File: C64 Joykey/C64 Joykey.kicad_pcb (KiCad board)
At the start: 2 copper layers, 99.7 x 74.9 mm, 47 parts, among them J1 Port_1, J2 Port_2, M1 Mounting, M2 Mounting, M3 Mounting, M4 Mounting, Q1 2N3904, SW1 FIRE1, SW2 FIRE2, SW3 FIRE3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

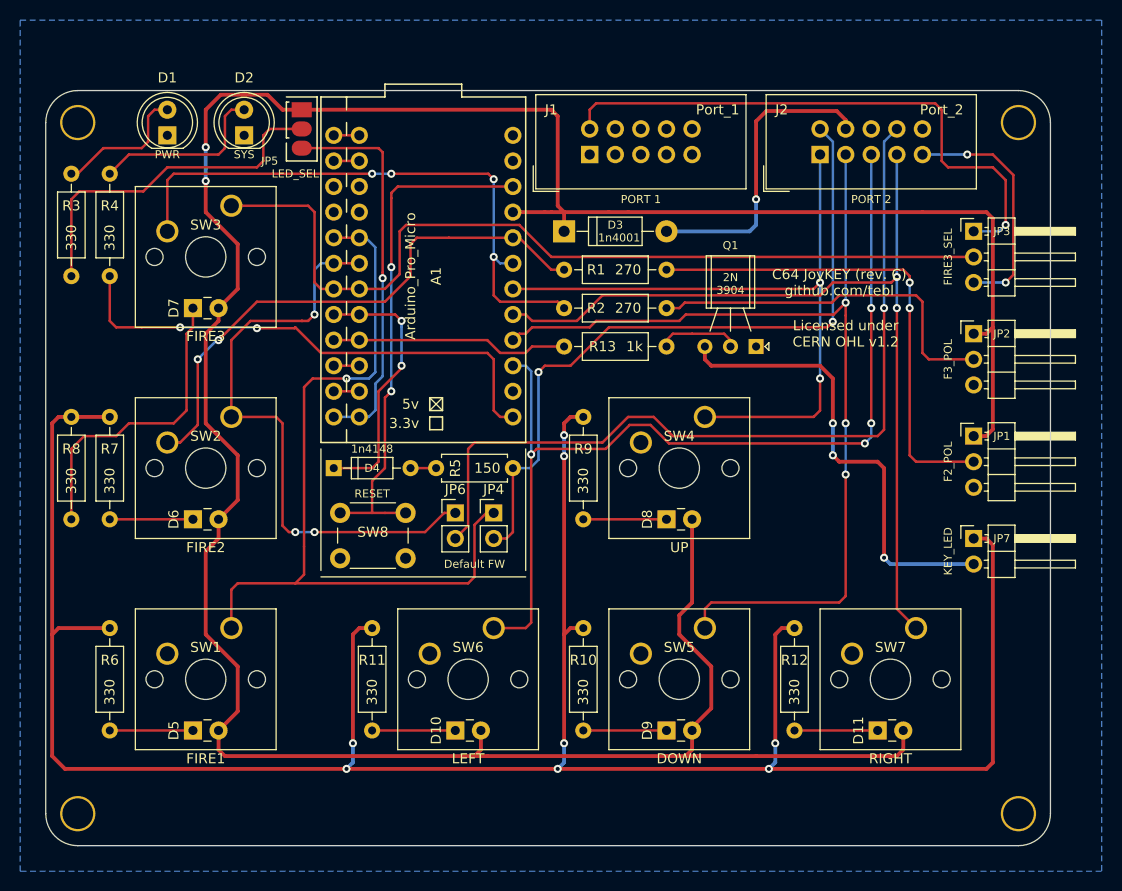
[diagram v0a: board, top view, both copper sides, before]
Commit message: Flipped MX-switches
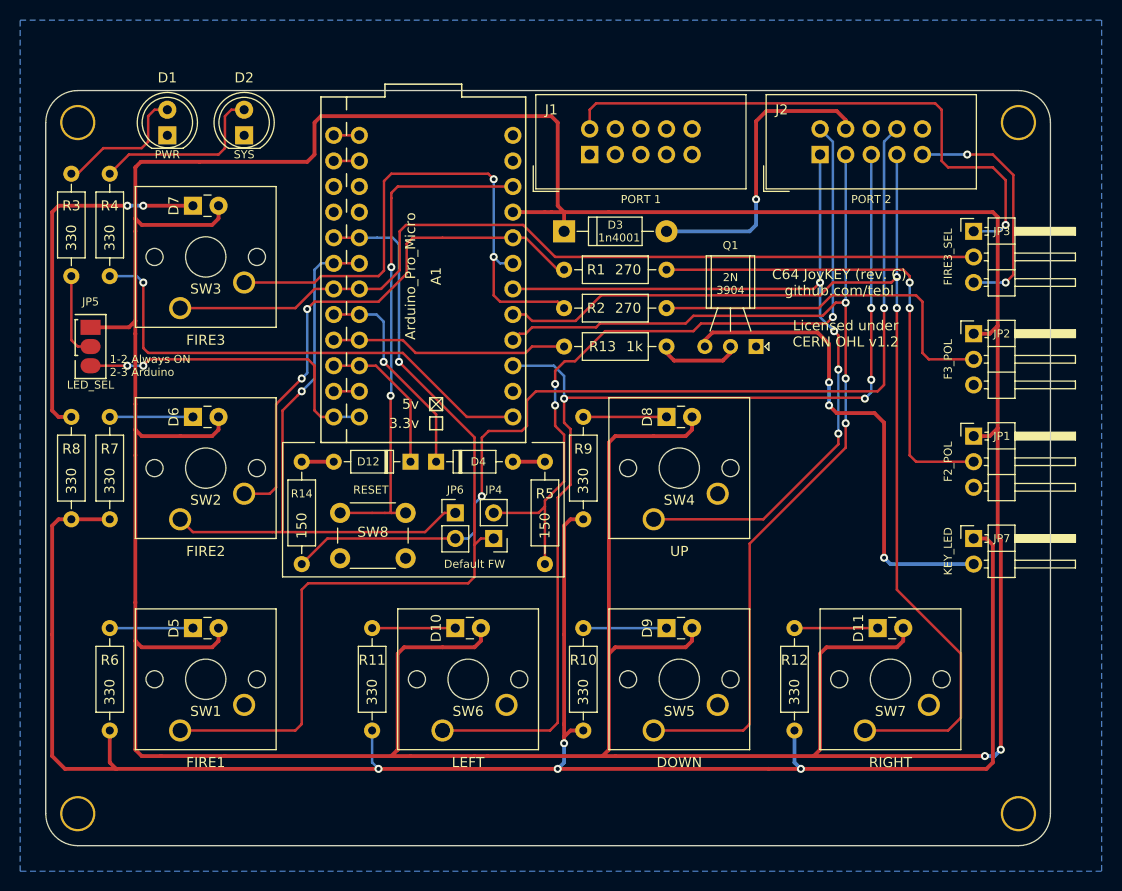
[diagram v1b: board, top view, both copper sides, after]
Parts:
- added D12: 1n4148, Diode_THT:D_DO-35_SOD27_P7.62mm_Horizontal, F.Cu at (177.2, 119.4)
- added R14: 150, Resistor_THT:R_Axial_DIN0207_L6.3mm_D2.5mm_P10.16mm_Horizontal, F.Cu at (166.4, 119.4)
- D4: footprint Diodes_THT:D_DO-35_SOD27_P7.62mm_Horizontal -> Diode_THT:D_DO-35_SOD27_P7.62mm_Horizontal
- R5: footprint Resistor_THT:R_Axial_DIN0207_L6.3mm_D2.5mm_P7.62mm_Horizontal -> Resistor_THT:R_Axial_DIN0207_L6.3mm_D2.5mm_P10.16mm_Horizontal
- moved JP5 30.1 mm to (145.4, 106.0)
- moved SW5 11.4 mm to (201.3, 146.1), turned to 180 degrees
- moved SW7 11.4 mm to (222.2, 146.1), turned to 180 degrees
- moved SW1 11.4 mm to (154.3, 146.1), turned to 180 degrees
- moved SW6 11.4 mm to (180.3, 146.1), turned to 180 degrees
- moved SW4 11.4 mm to (201.3, 125.1), turned to 180 degrees
- moved SW2 11.4 mm to (154.3, 125.1), turned to 180 degrees
- moved SW3 11.4 mm to (154.3, 104.1), turned to 180 degrees
- moved R5 10.8 mm to (190.5, 119.4), turned to 270 degrees
- moved D4 10.2 mm to (179.7, 119.4)
- moved D10 10.2 mm to (181.6, 135.9)
- moved D11 10.2 mm to (223.5, 135.9)
- moved D5 10.2 mm to (155.6, 135.9)
- moved D9 10.2 mm to (202.6, 135.9)
- moved R10 10.2 mm to (194.3, 135.9), turned to 270 degrees
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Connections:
- net Net-(A1-Pad12) renamed /PWR
- net Net-(A1-Pad13) renamed /SYS
- net Net-(A1-Pad9) renamed /UNDERGLOW
- A1 pad 10: Net-(A1-Pad10) -> /FIRE2_OUT
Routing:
- net VCC: track 292.3 -> 436.0 mm
- net Net-(JP7-Pad1): track 233.3 -> 187.7 mm, vias 8 -> 4
- net Net-(JP5-Pad2): track 34.9 -> 8.52 mm
- net P2_RIGHT: track 88.0 -> 108.8 mm
- net /FIRE2_OUT: track 0.00 -> 15.1 mm
- net P2_FIRE2: track 83.4 -> 97.6 mm, vias 1 -> 2
- net P2_UP: track 67.8 -> 81.7 mm, vias 2 -> 4
- net P2_LEFT: track 94.9 -> 107.0 mm
- net P2_DOWN: track 94.8 -> 104.8 mm
- net /FIRE1_IN: track 80.4 -> 88.4 mm
- net /PWR: track 38.5 -> 31.9 mm, vias 1 -> 2
- net Net-(D7-Pad1): track 30.4 -> 36.1 mm, vias 0 -> 2
- net /FIRE1_OUT: track 26.6 -> 21.3 mm, vias 2 -> 1
- net P2_FIRE1: track 71.0 -> 75.4 mm, vias 2 -> 3
- net FIRE3_POL: track 59.2 -> 55.9 mm, vias 4 -> 2
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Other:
- board text added: "1-2 Always ON 2-3 Arduino"
- board text removed: "1"
- board text removed: "2"
- board text removed: "3"
- board text removed: "PWR SELECT (2-3 for Arduino)"

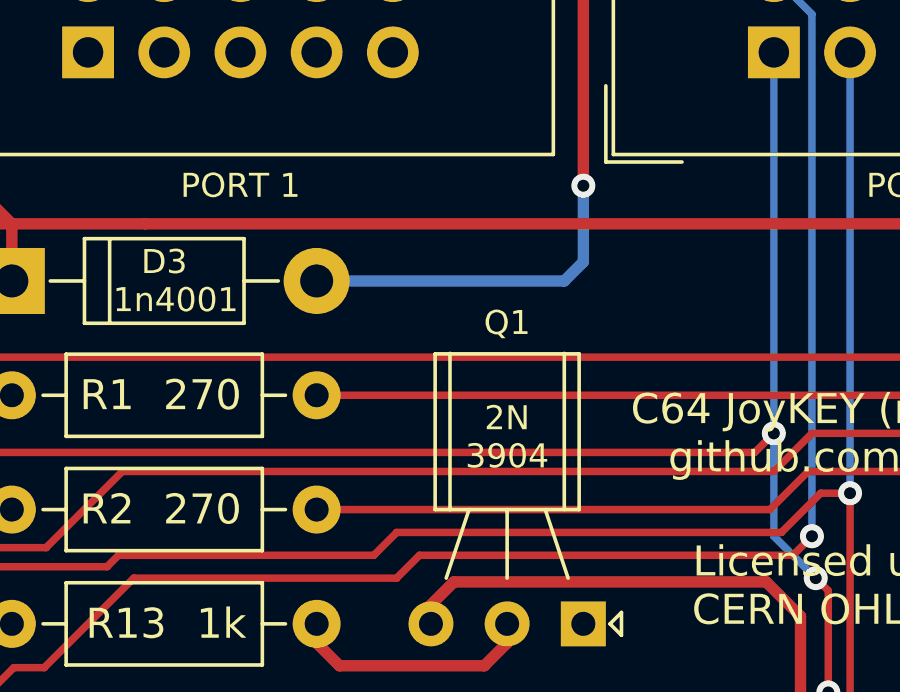
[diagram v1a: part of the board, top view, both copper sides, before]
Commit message: Added VCC_EN jumper
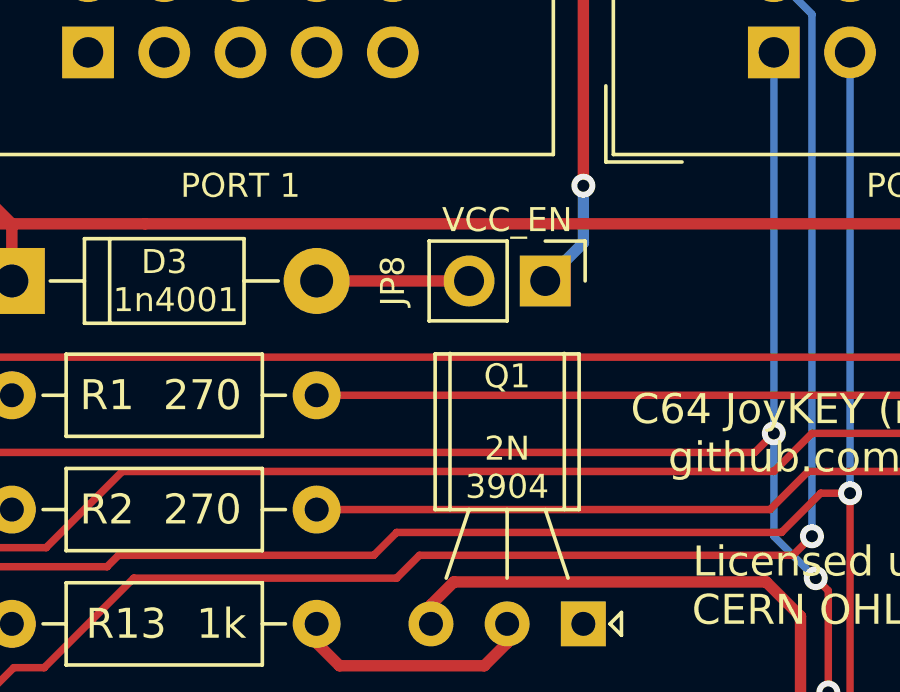
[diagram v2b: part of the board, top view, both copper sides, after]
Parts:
- added JP8: VCC_EN, Connector_PinHeader_2.54mm:PinHeader_1x02_P2.54mm_Vertical, F.Cu at (210.2, 96.5)
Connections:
- J2 pad 7: Net-(D3-Pad2) -> Net-(J2-Pad7)
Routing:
- net Net-(D3-Pad2): track 30.0 -> 5.08 mm, vias 1 -> 0
- net Net-(J2-Pad7): track 0.00 -> 22.0 mm, vias 0 -> 1
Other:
- board text added: "VCC_EN"

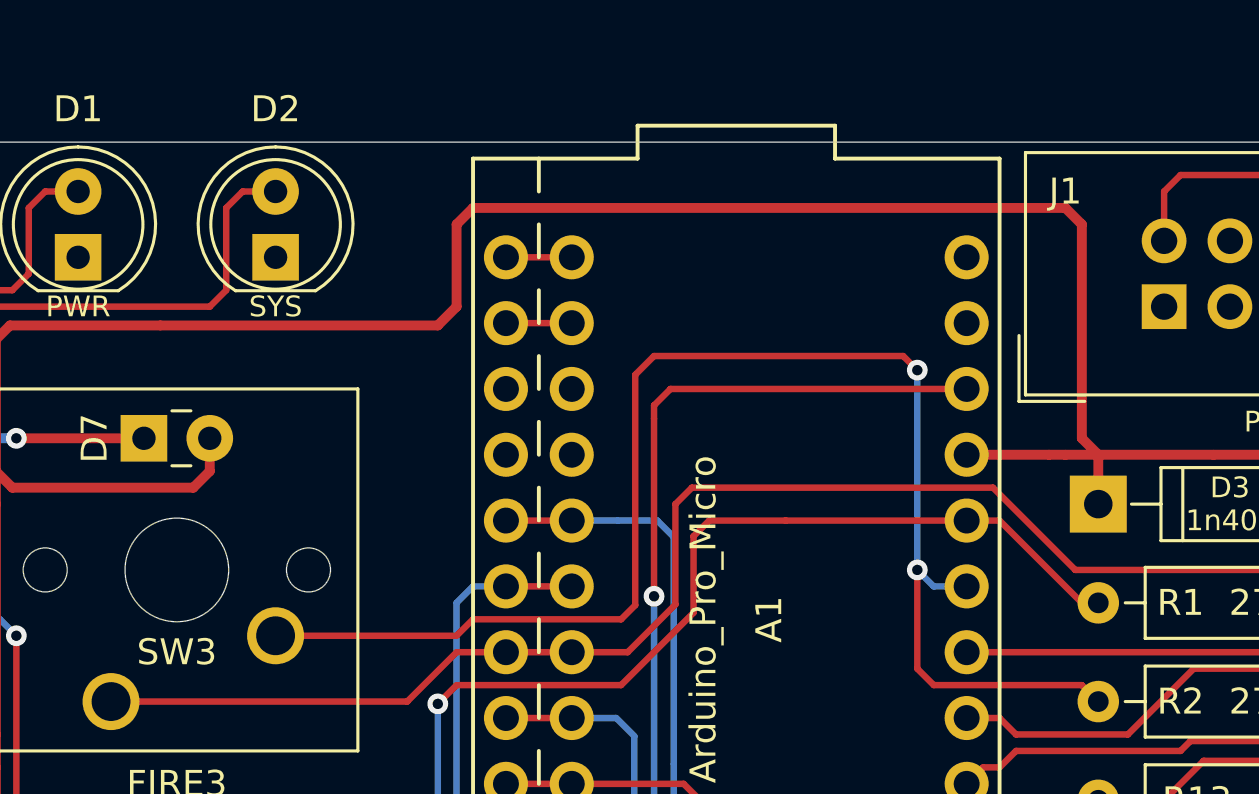
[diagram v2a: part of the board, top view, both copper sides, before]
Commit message: Added ARD_EN jumper
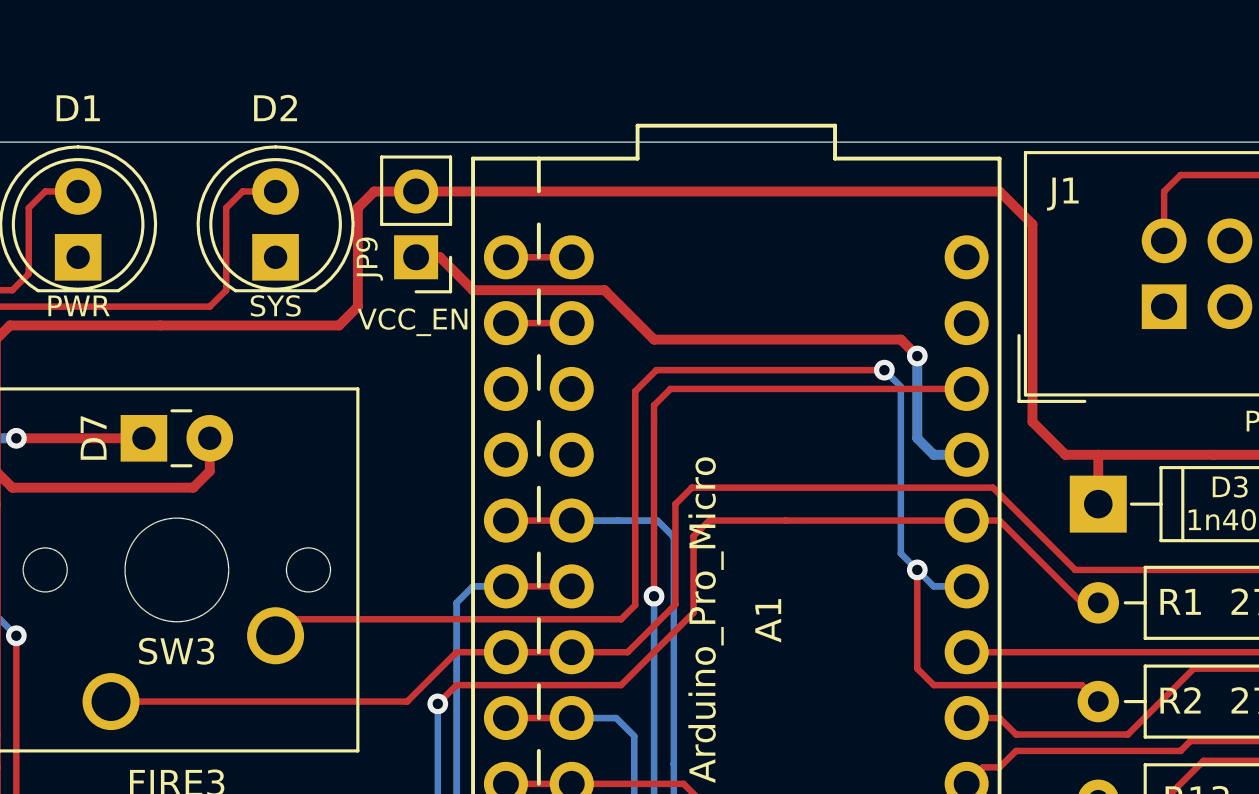
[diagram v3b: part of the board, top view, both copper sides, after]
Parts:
- added JP9: VCC_EN, Connector_PinHeader_2.54mm:PinHeader_1x02_P2.54mm_Vertical, F.Cu at (166.1, 87.0)
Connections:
- A1 pad 21: VCC -> Net-(A1-Pad21)
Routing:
- net Net-(A1-Pad21): track 0.00 -> 26.3 mm, vias 0 -> 1
- net VCC: track 436.0 -> 431.5 mm
- net FIRE3_POL: track 55.9 -> 54.3 mm
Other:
- board text added: "ARD_EN"

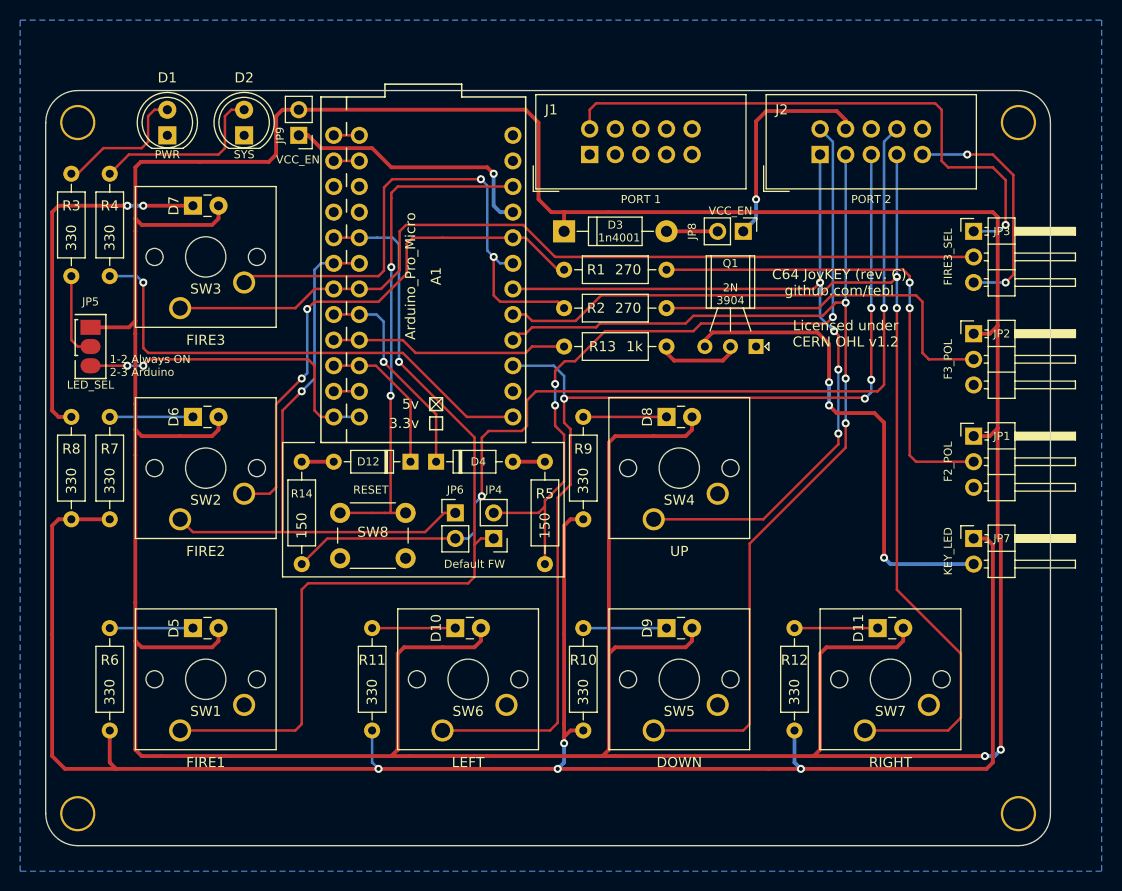
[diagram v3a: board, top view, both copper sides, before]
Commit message: Added 10k resistors to isolate unpowered Arduino
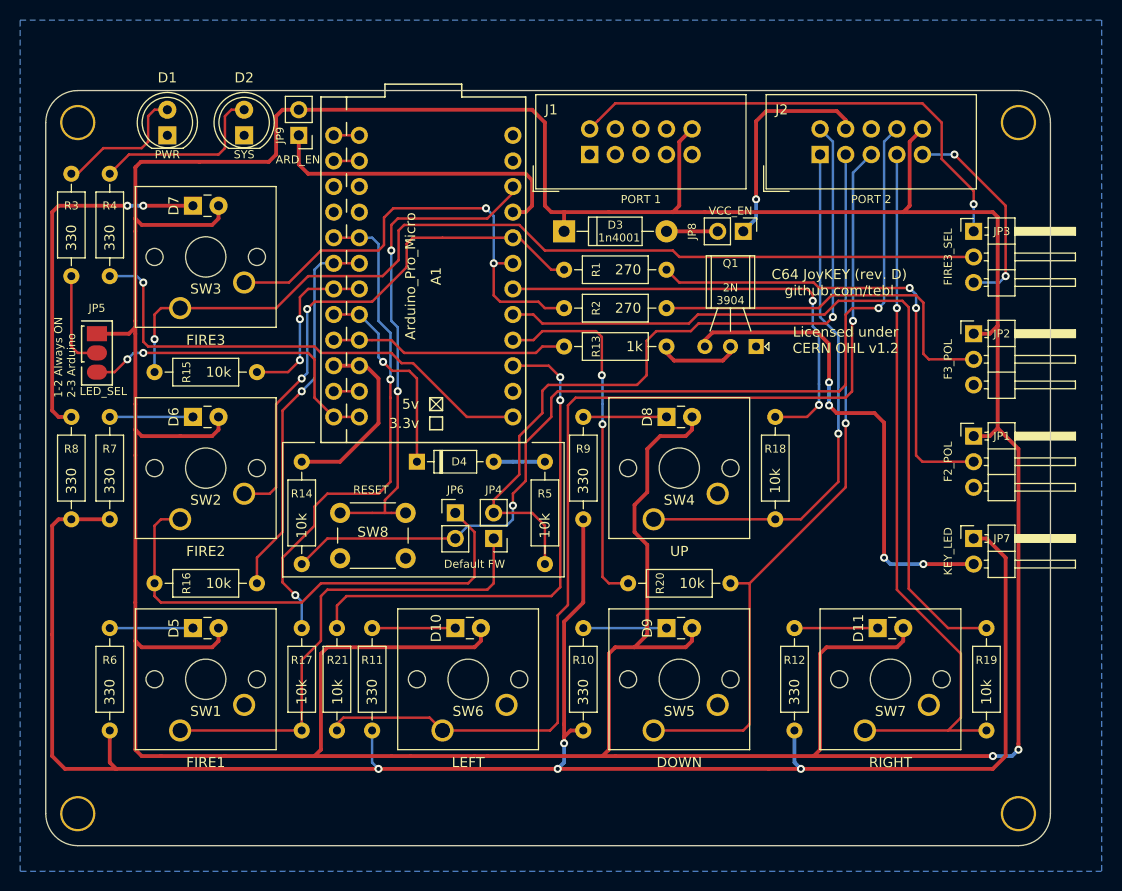
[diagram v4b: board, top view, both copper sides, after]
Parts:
- removed D12: 1n4148, Diode_THT:D_DO-35_SOD27_P7.62mm_Horizontal
- added R15: 10k, Resistor_THT:R_Axial_DIN0207_L6.3mm_D2.5mm_P10.16mm_Horizontal, F.Cu at (161.9, 110.5)
- added R16: 10k, Resistor_THT:R_Axial_DIN0207_L6.3mm_D2.5mm_P10.16mm_Horizontal, F.Cu at (161.9, 131.4)
- added R17: 10k, Resistor_THT:R_Axial_DIN0207_L6.3mm_D2.5mm_P10.16mm_Horizontal, F.Cu at (166.4, 135.9)
- added R18: 10k, Resistor_THT:R_Axial_DIN0207_L6.3mm_D2.5mm_P10.16mm_Horizontal, F.Cu at (213.4, 125.1)
- added R19: 10k, Resistor_THT:R_Axial_DIN0207_L6.3mm_D2.5mm_P10.16mm_Horizontal, F.Cu at (234.3, 146.1)
- added R20: 10k, Resistor_THT:R_Axial_DIN0207_L6.3mm_D2.5mm_P10.16mm_Horizontal, F.Cu at (208.9, 131.4)
- added R21: 10k, Resistor_THT:R_Axial_DIN0207_L6.3mm_D2.5mm_P10.16mm_Horizontal, F.Cu at (169.9, 146.1)
- JP9: value VCC_EN -> ARD_EN
- R14, R5: value 150 -> 10k
- moved D4 1.91 mm to (177.8, 119.4)
- moved JP5 0.90 mm to (146.1, 106.7)
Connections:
- A1 pad 15: P2_LEFT -> Net-(A1-Pad15)
- A1 pad 16: P2_DOWN -> Net-(A1-Pad16)
- A1 pad 17: P2_RIGHT -> Net-(A1-Pad17)
- A1 pad 18: P2_UP -> Net-(A1-Pad18)
- J1 pad 10: (no net) -> VCC
- J2 pad 10: (no net) -> VCC
- JP3 pad 2: /FIRE3_IN -> Net-(JP3-Pad2)
- JP4 pad 1: /FIRE1_IN -> Net-(JP4-Pad1)
- JP6 pad 1: /FIRE2_IN -> Net-(JP6-Pad1)
- R14 pad 1: Net-(D12-Pad2) -> /FIRE2_OUT
- SW1 pad 1: /FIRE1_IN -> Net-(JP4-Pad1)
- SW2 pad 1: /FIRE2_IN -> Net-(JP6-Pad1)
- SW3 pad 1: /FIRE3_IN -> Net-(JP3-Pad2)
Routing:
- net Net-(JP3-Pad2): track 0.00 -> 93.7 mm, vias 0 -> 1
- net Net-(A1-Pad17): track 0.00 -> 78.1 mm
- net /FIRE3_IN: track 85.7 -> 17.2 mm, vias 0 -> 2
- net Net-(A1-Pad15): track 0.00 -> 51.1 mm, vias 0 -> 2
- net Net-(JP6-Pad1): track 0.00 -> 50.0 mm
- net Net-(JP4-Pad1): track 0.00 -> 49.2 mm
- net Net-(A1-Pad18): track 0.00 -> 46.1 mm, vias 0 -> 2
- net /FIRE1_IN: track 88.4 -> 51.5 mm, vias 1 -> 2
- net P2_RIGHT: track 108.8 -> 72.4 mm, vias 2 -> 1
- net Net-(A1-Pad16): track 0.00 -> 36.1 mm, vias 0 -> 2
- net P2_DOWN: track 104.8 -> 72.2 mm, vias 3 -> 1
- net P2_UP: track 81.7 -> 53.1 mm, vias 4 -> 1
- net VCC: track 431.5 -> 456.2 mm
- net /FIRE2_IN: track 60.7 -> 38.2 mm
- net P1_FIRE1: track 57.5 -> 48.9 mm
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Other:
- board text added: "C64 JoyKEY (rev. D) github.com/tebl"
- board text removed: "C64 JoyKEY (rev. C) github.com/tebl"

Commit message: Route new tracks and export gerbers
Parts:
- added G***: LOGO, logo:c64_joykey, F.Cu at (221.6, 103.5)
- added SW10: P1_FIRE2, Button_Switch_THT:SW_Tactile_SPST_Angled_PTS645Vx31-2LFS, F.Cu at (167.4, 154.7)
- added SW11: P1_FIRE3, Button_Switch_THT:SW_Tactile_SPST_Angled_PTS645Vx31-2LFS, F.Cu at (179.4, 154.7)
- added SW9: P1_FIRE1, Button_Switch_THT:SW_Tactile_SPST_Angled_PTS645Vx31-2LFS, F.Cu at (155.4, 154.7)
- SW1: value FIRE1 -> P2_FIRE1
- SW2: value FIRE2 -> P2_FIRE2
- SW3: value FIRE3 -> P2_FIRE3
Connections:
- J1 pad 5: (no net) -> P1_FIRE3
- J1 pad 9: (no net) -> P1_FIRE2
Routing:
- net P1_FIRE2: track 0.00 -> 175.1 mm, vias 0 -> 2
- net P1_FIRE3: track 0.00 -> 160.1 mm, vias 0 -> 1
- net P1_FIRE1: track 48.9 -> 193.5 mm, vias 1 -> 2
- net FIRE3_POL: track 47.1 -> 142.7 mm, vias 2 -> 4
- net FIRE2_POL: track 53.5 -> 118.1 mm, vias 2 -> 4
- net Net-(JP7-Pad1): track 188.4 -> 178.8 mm
- net VCC: track 456.2 -> 455.0 mm
- net P2_FIRE3: track 20.8 -> 21.2 mm, vias 2 -> 1
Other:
- board text added: "P1 F1"
- board text added: "P1 F2"
- board text added: "P1 F3"
- board text added: "PCB Revision E github.com/tebl"
- board text removed: "Atari_7800* N/C N/C GND"
- board text removed: "C64 JoyKEY (rev. D) github.com/tebl"
- board text removed: "SMS* N/C N/C GND"
- board text removed: "Sinclair* N/C N/C N/C"
